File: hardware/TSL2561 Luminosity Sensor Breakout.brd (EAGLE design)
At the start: 15.2 x 18.4 mm, 14 parts, among them U1 TSL2561T

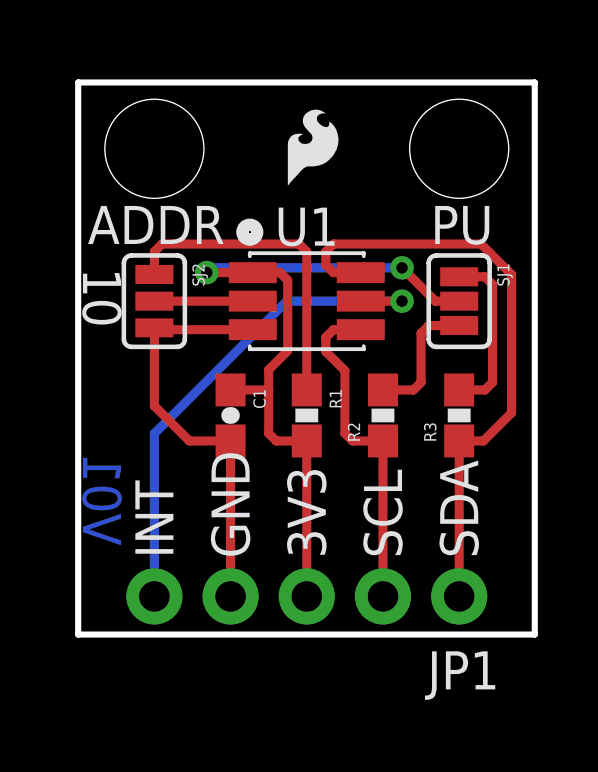
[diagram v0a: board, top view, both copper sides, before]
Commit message: Updated prototype to V02
Per discussion with Pete L, replaced T package with FN package.
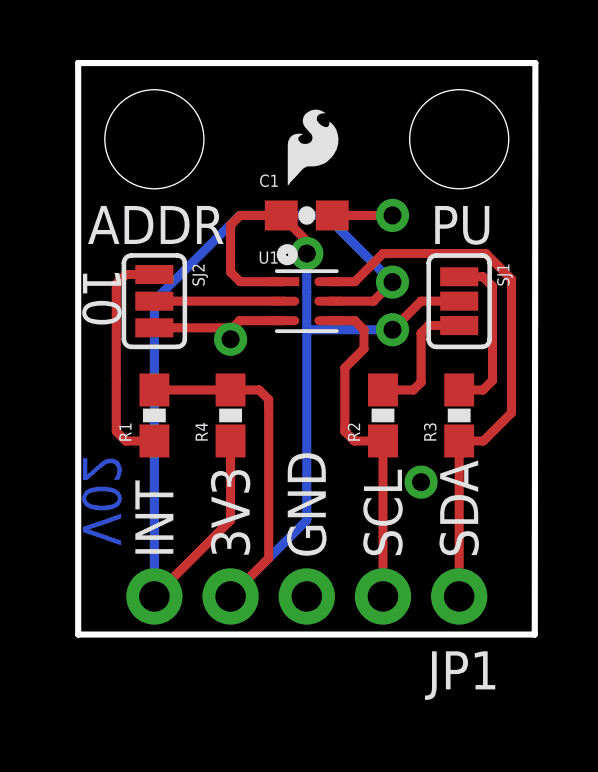
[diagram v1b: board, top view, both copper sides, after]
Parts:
- added R4: 10K, SparkFun-Resistors:0603-RES
- U1: value TSL2561T -> TSL2561FN; device mike-temp:TMB-6 -> mike-temp:FN-6
- moved C1 7.13 mm to (7.62, 14.0), turned to 0 degrees
- moved R1 5.08 mm to (2.54, 7.30), turned to 90 degrees
- moved STANDOFF1 0.32 mm to (2.54, 16.5)
- moved STANDOFF2 0.32 mm to (12.7, 16.5)
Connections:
- net 3.3V: now also JP1.4, R4.2; no longer JP1.3
- net GND: now also JP1.3; no longer JP1.4
- net INT: now also R4.1
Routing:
- net INT: track 16.9 -> 28.5 mm
- net 3.3V: track 24.9 -> 35.9 mm
- net GND: track 14.2 -> 6.47 mm, vias 0 -> 3
- net N$2: track 10.7 -> 7.72 mm
- net SDA: track 20.4 -> 18.6 mm
- net N$3: track 3.28 -> 4.30 mm
- added copper zone on layer 1, net GND
- added copper zone on layer 16, net GND
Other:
- board size 15.2 x 18.4 mm -> 15.2 x 19.1 mm
- board text added: "0.125 x 2"
- board text added: "V02"
- board text removed: "V01"
